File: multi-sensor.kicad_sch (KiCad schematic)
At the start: 6 parts, among them J1 AHT20, J2 Adafruit 189, U1 ESP32-C3-SuperMini

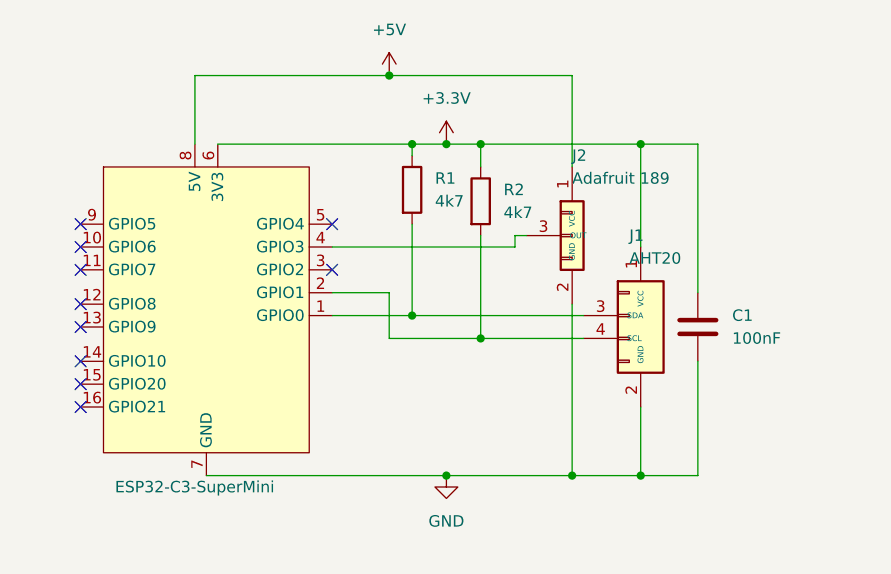
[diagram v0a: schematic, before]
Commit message: Add BH1750 lux sensor
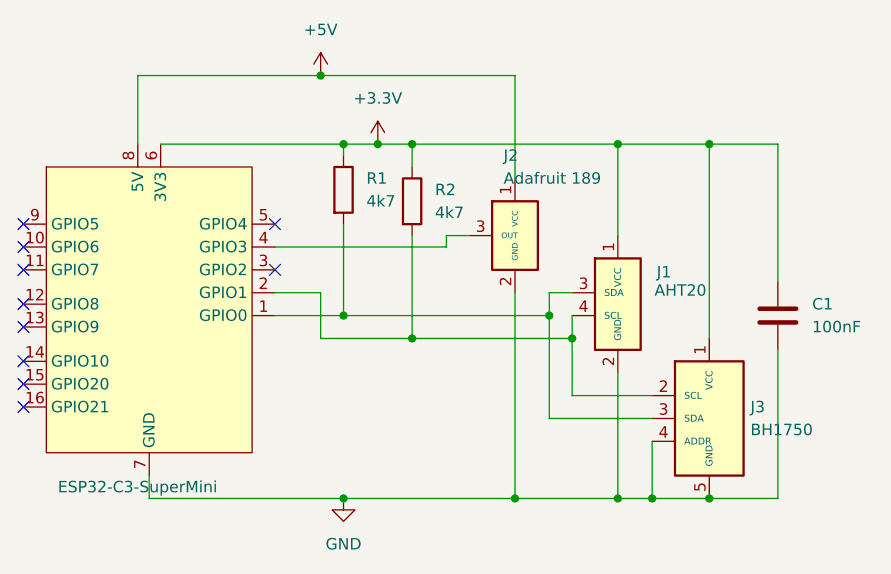
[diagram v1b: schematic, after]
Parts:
- added J3: BH1750, Package_DFN_QFN:TDFN-10-1EP_2x3mm_P0.5mm_EP0.9x2mm, symbol Connector_Generic:Conn_01x05
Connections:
- net +3.3V: now also J3.1 (VCC)
- net GND: now also J3.4 (ADDR), J3.5 (GND)
- net at J1.4 (SCL), R2.2, U1.2 (GPIO1): now also J3.2 (SCL)
- net at J1.3 (SDA), R1.2, U1.1 (GPIO0): now also J3.3 (SDA)
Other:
- moved on the sheet: C1, R1, R2
